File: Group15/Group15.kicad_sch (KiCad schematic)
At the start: 0 parts

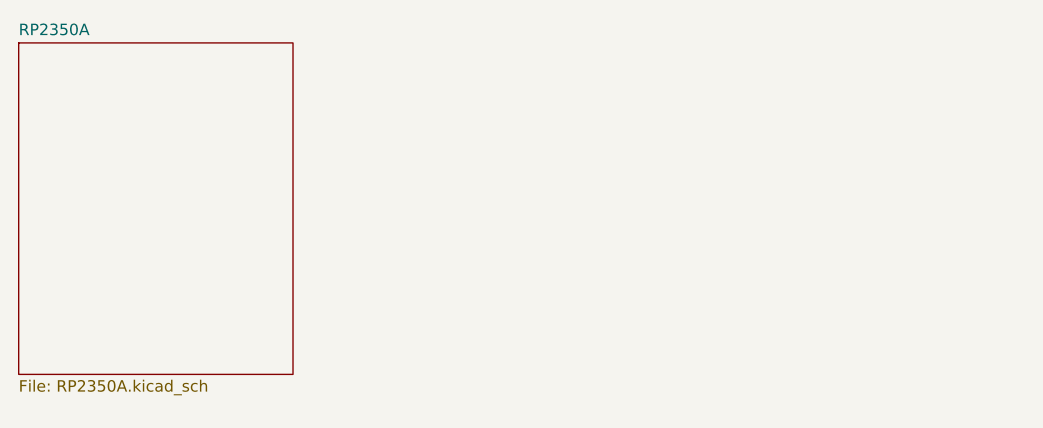
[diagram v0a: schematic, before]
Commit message: USB_C added
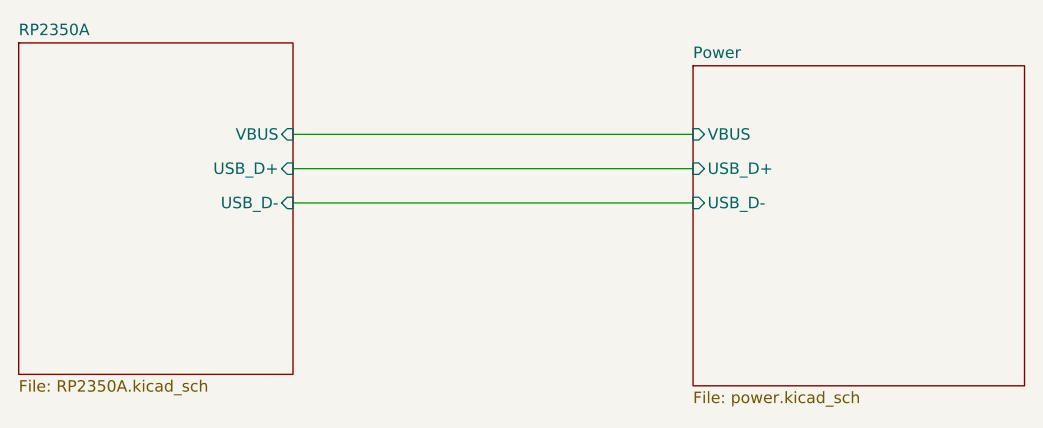
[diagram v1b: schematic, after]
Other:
- added sheet Power (power.kicad_sch)
- sheet RP2350A ports: added USB_D+, USB_D-, VBUS; removed none
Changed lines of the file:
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@@
 		(date "2026-10-24")
+	)
+	(wire
+		(pts
+			(xy 82.55 60.96) (xy 127 60.96)
+		)
+		(stroke
+			(width 0)
+			(type default)
+		)
+	)
+	(wire
+		(pts
+			(xy 82.55 64.77) (xy 127 64.77)
+		)
+		(stroke
+			(width 0)
+			(type default)
+		)
+	)
+	(wire
+		(pts
+			(xy 82.55 57.15) (xy 127 57.15)
+		)
+		(stroke
+			(width 0)
+			(type default)
+		)
+	)
+	(sheet
+		(at 127 49.53)
+		(size 36.83 35.56)
+		(exclude_from_sim no)
+		(in_bom yes)
+		(on_board yes)
+		(dnp no)
+		(fields_autoplaced yes)
+		(stroke
+			(width 0.1524)
+			(type solid)
+		)
+		(fill
+			(color 0 0 0 0)
+		)
+		(property "Sheetname" "Power"
+			(at 127 48.8184 0)
+			(show_name no)
+			(do_not_autoplace no)
+			(effects
+				(font
+					(size 1.27 1.27)
+				)
+				(justify left bottom)
+			)
+		)
+		(property "Sheetfile" "power.kicad_sch"
+			(at 127 85.6746 0)
+			(show_name no)
+			(do_not_autoplace no)
+			(effects
+				(font
+					(size 1.27 1.27)
+				)
+				(justify left top)
+			)
+		)
+		(pin "VBUS" input
+			(at 127 57.15 180)
+			(effects
+				(font
+					(size 1.27 1.27)
+				)
+				(justify left)
+			)
+		)
+		(pin "USB_D+" input
+			(at 127 60.96 180)
+			(effects
+				(font
+					(size 1.27 1.27)
+				)
+				(justify left)
+			)
+		)
+		(pin "USB_D-" input
+			(at 127 64.77 180)
+			(effects
+				(font
+					(size 1.27 1.27)
+				)
+				(justify left)
+			)
+		)
+		(instances
+			(project "Group15"
+				(path "/d18e2577-1276-4c0d-bdfd-a503d70bff69"
+					(page "3")
+				)
+			)
+		)
 	)
 	(sheet
@@
 			)
 		)
+		(pin "VBUS" input
+			(at 82.55 57.15 0)
+			(effects
+				(font
+					(size 1.27 1.27)
+				)
+				(justify right)
+			)
+		)
+		(pin "USB_D+" input
+			(at 82.55 60.96 0)
+			(effects
+				(font
+					(size 1.27 1.27)
+				)
+				(justify right)
+			)
+		)
+		(pin "USB_D-" input
+			(at 82.55 64.77 0)
+			(effects
+				(font
+					(size 1.27 1.27)
+				)
+				(justify right)
+			)
+		)
